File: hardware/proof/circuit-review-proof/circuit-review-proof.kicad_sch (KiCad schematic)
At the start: 54 parts, among them J1 MKDSN_1.5/3-5.08, J2 HEATER, J3 SENSOR_I2C, J4 SWD, J5 SENSE_IN, J6 5V_IN, Q1 BTA16-600B, Q2 BSS138, Q3 BSS138, U2 MOC3023M, U3 MCP1700T-3302E/TT, U4 MSPS003F4SPW20R, U5 TPS3823-33DBVR

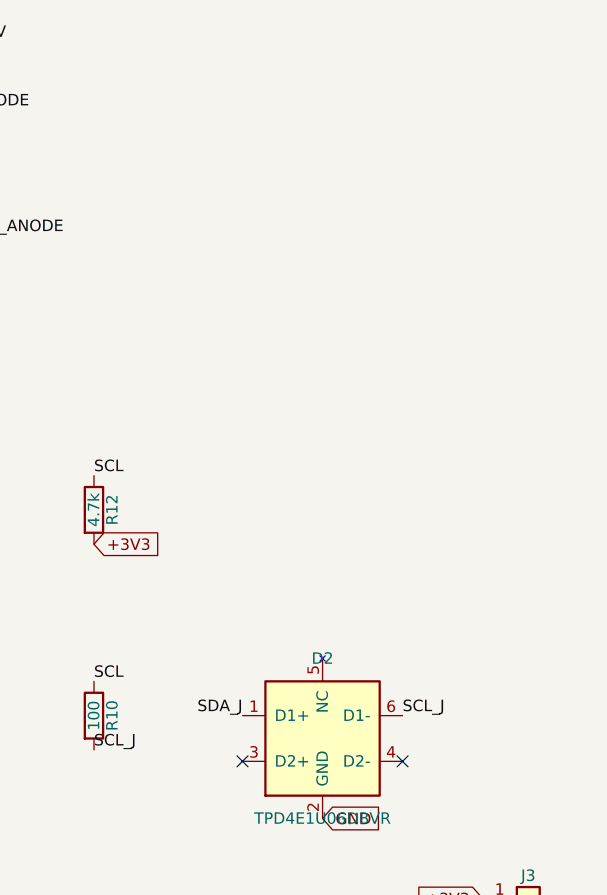
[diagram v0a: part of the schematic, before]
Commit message: fix(hardware): give the tracked proof designs the three fiducials a side with surface-mount parts needs [SOL-PRE-ORDER-CHECK-FIDUCIALS-AND-POLARITY-MARKS.C5]
Co-Authored-By: Claude Sonnet 5.5 <noreply@anthropic.com>
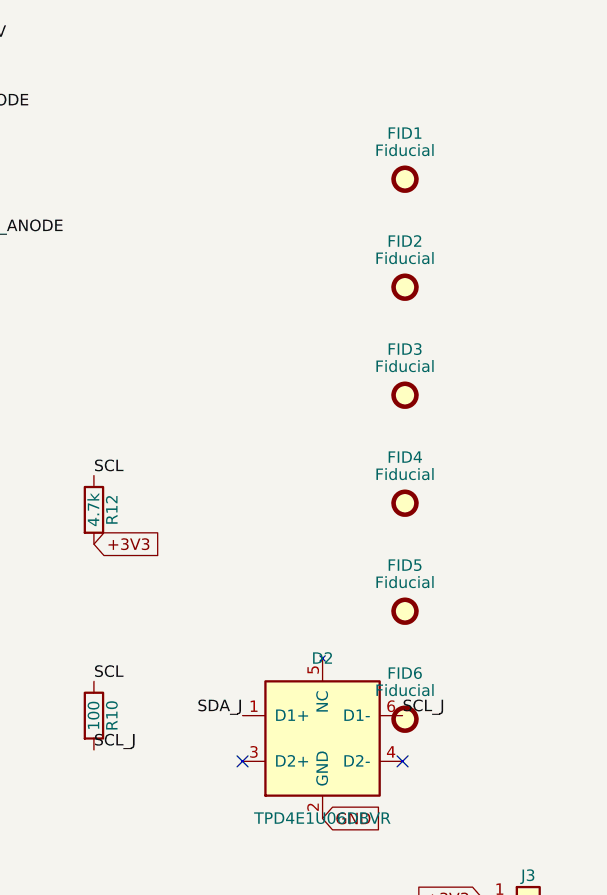
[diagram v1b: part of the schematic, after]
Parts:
- added FID1, FID2, FID3, FID4, FID5, FID6: Fiducial, Fiducial:Fiducial_1mm_Mask2mm, symbol Mechanical:Fiducial

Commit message: fix(hardware): circuit review proof ratings the derating rule can read, U4 at its datasheet maximum [SOL-PRE-ORDER-CHECK-DERATED-VOLTAGE-AND-PIN-LIMITS.C6]
Co-Authored-By: Claude Sonnet 5.5 <noreply@anthropic.com>
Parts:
- J1, J2: Rating 320V 8A -> 320VAC 8A
- JP1: Rating 300V 6A -> 300VAC 6A
- RV1: Rating 275Vrms -> 275VAC
- U4: Rating 3.8V -> 4.1V
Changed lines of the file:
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@@
 			)
 		)
-		(property "Rating" "320V 8A"
+		(property "Rating" "320VAC 8A"
 			(at 30.48 45.72 0)
 			(hide yes)
@@
 			)
 		)
-		(property "Rating" "300V 6A"
+		(property "Rating" "300VAC 6A"
 			(at 99.06 40.64 0)
 			(hide yes)
@@
 			)
 		)
-		(property "Rating" "275Vrms"
+		(property "Rating" "275VAC"
 			(at 121.92 40.64 0)
 			(hide yes)
@@
 			)
 		)
-		(property "Rating" "320V 8A"
+		(property "Rating" "320VAC 8A"
 			(at 167.64 99.06 0)
 			(hide yes)
@@
 			)
 		)
-		(property "Rating" "3.8V"
+		(property "Rating" "4.1V"
 			(at 274.32 71.12 0)
 			(hide yes)
